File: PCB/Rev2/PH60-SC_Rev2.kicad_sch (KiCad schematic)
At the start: 43 parts, among them J1 USB_C_Receptacle_USB2.0_14P, J2 Conn_01x02_Pin, J3 Conn_01x02_Pin, U1 nRF52840, X1 32.768kHz, X2 Crystal_Generic

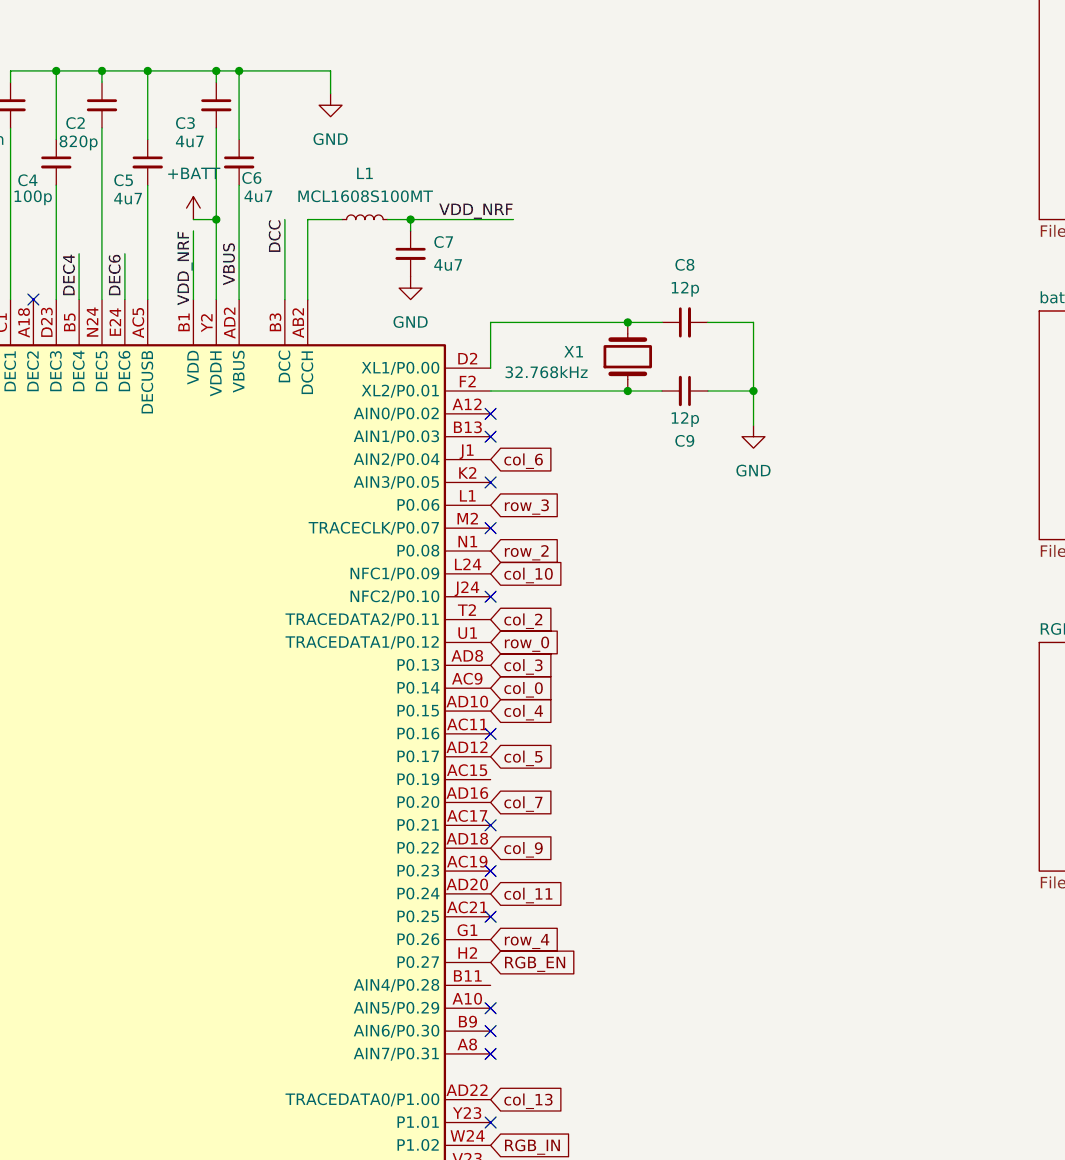
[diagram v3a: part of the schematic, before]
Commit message: 电源模块布局及drc
修改52840的vddh，将batt修改为vdd，TPS2116DRL布局与简单drc，rgb_vdd布局仍需修改
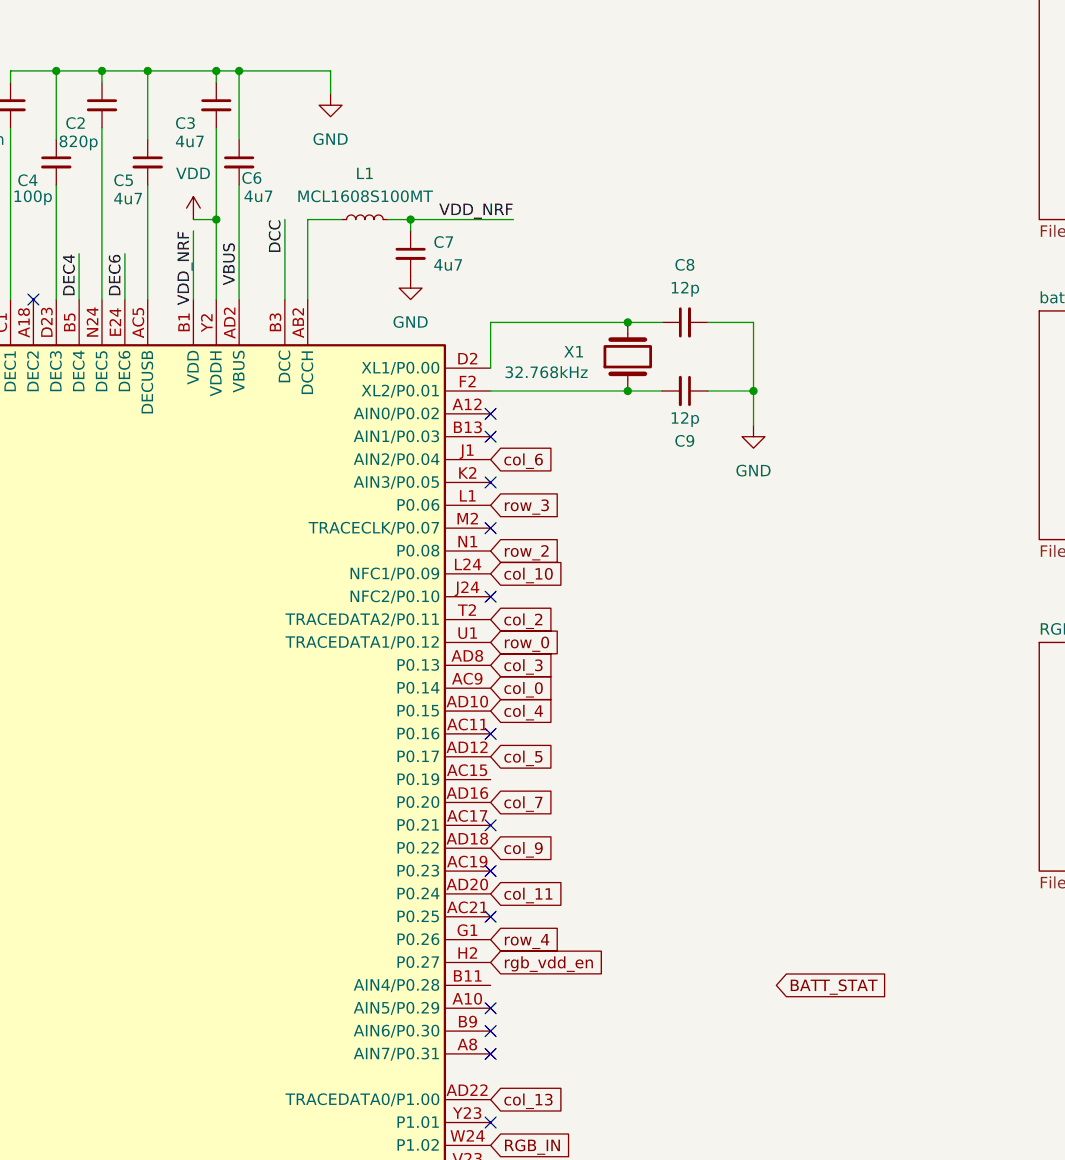
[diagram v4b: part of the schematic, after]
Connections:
- net +BATT renamed VDD
- net RGB_EN renamed rgb_vdd_en
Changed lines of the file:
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@@
 		)
 	)
-	(global_label "RGB_EN"
-		(shape input)
-		(at 256.54 152.4 0)
-		(fields_autoplaced yes)
-		(effects
-			(font
-				(size 1.27 1.27)
-			)
-			(justify left)
-		)
-		(property "Intersheetrefs" "${INTERSHEET_REFS}"
-			(at 266.7823 152.4 0)
-			(effects
-				(font
-					(size 1.27 1.27)
-				)
-				(justify left)
-				(hide yes)
-			)
-		)
-	)
 	(global_label "col_12"
 		(shape input)
@@
 		)
 	)
+	(global_label "BATT_STAT"
+		(shape input)
+		(at 288.29 154.94 0)
+		(fields_autoplaced yes)
+		(effects
+			(font
+				(size 1.27 1.27)
+			)
+			(justify left)
+		)
+		(property "Intersheetrefs" "${INTERSHEET_REFS}"
+			(at 300.7699 154.94 0)
+			(effects
+				(font
+					(size 1.27 1.27)
+				)
+				(justify left)
+				(hide yes)
+			)
+		)
+	)
+	(global_label "rgb_vdd_en"
+		(shape input)
+		(at 256.54 152.4 0)
+		(fields_autoplaced yes)
+		(effects
+			(font
+				(size 1.27 1.27)
+			)
+			(justify left)
+		)
+		(property "Intersheetrefs" "${INTERSHEET_REFS}"
+			(at 270.0478 152.4 0)
+			(effects
+				(font
+					(size 1.27 1.27)
+				)
+				(justify left)
+				(hide yes)
+			)
+		)
+	)
 	(symbol
 		(lib_id "Device:C_Small")
@@
 		(dnp no)
 		(fields_autoplaced yes)
-		(property "Reference" "#PWR015"
+		(property "Reference" "#PWR016"
 			(at 154.94 262.89 0)
 			(effects
@@
 			(project "PH64lite"
 				(path "/dca0f898-8fdb-4522-a51d-f4f4238906e7"
-					(reference "#PWR015")
+					(reference "#PWR016")
 					(unit 1)
 				)
@@
 		(dnp no)
 		(fields_autoplaced yes)
-		(property "Reference" "#PWR016"
+		(property "Reference" "#PWR017"
 			(at 224.79 266.7 0)
 			(effects
@@
 			(project "PH64lite"
 				(path "/dca0f898-8fdb-4522-a51d-f4f4238906e7"
-					(reference "#PWR016")
+					(reference "#PWR017")
 					(unit 1)
 				)
@@
 		(dnp no)
 		(fields_autoplaced yes)
-		(property "Reference" "#PWR013"
+		(property "Reference" "#PWR014"
 			(at 85.09 218.44 0)
 			(effects
@@
 			(project "PH60S lite"
 				(path "/dca0f898-8fdb-4522-a51d-f4f4238906e7"
-					(reference "#PWR013")
+					(reference "#PWR014")
 					(unit 1)
 				)
@@
 		(dnp no)
 		(fields_autoplaced yes)
-		(property "Reference" "#PWR06"
+		(property "Reference" "#PWR07"
 			(at 35.56 105.41 0)
 			(effects
@@
 			(project "PH64lite"
 				(path "/dca0f898-8fdb-4522-a51d-f4f4238906e7"
-					(reference "#PWR06")
-					(unit 1)
-				)
-			)
-		)
-	)
-	(symbol
-		(lib_id "power:+BATT")
-		(at 223.52 69.85 0)
-		(unit 1)
-		(exclude_from_sim no)
-		(in_bom yes)
-		(on_board yes)
-		(dnp no)
-		(fields_autoplaced yes)
-		(property "Reference" "#PWR022"
-			(at 223.52 73.66 0)
-			(effects
-				(font
-					(size 1.27 1.27)
-				)
-				(hide yes)
-			)
-		)
-		(property "Value" "+BATT"
-			(at 223.52 64.77 0)
-			(effects
-				(font
-					(size 1.27 1.27)
-				)
-			)
-		)
-		(property "Footprint" ""
-			(at 223.52 69.85 0)
-			(effects
-				(font
-					(size 1.27 1.27)
-				)
-				(hide yes)
-			)
-		)
-		(property "Datasheet" ""
-			(at 223.52 69.85 0)
-			(effects
-				(font
-					(size 1.27 1.27)
-				)
-				(hide yes)
-			)
-		)
-		(property "Description" "Power symbol creates a global label with name \"+BATT\""
-			(at 223.52 69.85 0)
-			(effects
-				(font
-					(size 1.27 1.27)
-				)
-				(hide yes)
-			)
-		)
-		(pin "1"
-		)
-		(instances
-			(project "PH60-SC_Rev2"
-				(path "/dca0f898-8fdb-4522-a51d-f4f4238906e7"
-					(reference "#PWR022")
+					(reference "#PWR07")
 					(unit 1)
 				)
@@
 		(dnp no)
 		(fields_autoplaced yes)
-		(property "Reference" "#PWR014"
+		(property "Reference" "#PWR015"
 			(at 220.98 232.41 0)
 			(effects
@@
 			(project ""
 				(path "/dca0f898-8fdb-4522-a51d-f4f4238906e7"
-					(reference "#PWR014")
+					(reference "#PWR015")
 					(unit 1)
 				)
@@
 		(dnp no)
 		(fields_autoplaced yes)
-		(property "Reference" "#PWR012"
+		(property "Reference" "#PWR013"
 			(at 175.26 210.82 0)
 			(effects
@@
 			(project "PH64lite"
 				(path "/dca0f898-8fdb-4522-a51d-f4f4238906e7"
-					(reference "#PWR012")
+					(reference "#PWR013")
 					(unit 1)
 				)
@@
 		(dnp no)
 		(fields_autoplaced yes)
-		(property "Reference" "#PWR08"
+		(property "Reference" "#PWR09"
 			(at 158.75 163.83 0)
 			(effects
@@
 			(project "PH64lite"
 				(path "/dca0f898-8fdb-4522-a51d-f4f4238906e7"
-					(reference "#PWR08")
+					(reference "#PWR09")
 					(unit 1)
 				)
@@
 		(dnp no)
 		(fields_autoplaced yes)
-		(property "Reference" "#PWR019"
+		(property "Reference" "#PWR011"
 			(at 350.52 184.15 0)
 			(effects
@@
 			(project "PH60-SC_Rev2"
 				(path "/dca0f898-8fdb-4522-a51d-f4f4238906e7"
-					(reference "#PWR019")
+					(reference "#PWR011")
 					(unit 1)
 				)
@@
 		(dnp no)
 		(fields_autoplaced yes)
-		(property "Reference" "#PWR011"
+		(property "Reference" "#PWR012"
 			(at 363.22 191.77 0)
 			(effects
@@
 			(project ""
 				(path "/dca0f898-8fdb-4522-a51d-f4f4238906e7"
-					(reference "#PWR011")
+					(reference "#PWR012")
 					(unit 1)
 				)
@@
 		(dnp no)
 		(fields_autoplaced yes)
-		(property "Reference" "#PWR04"
+		(property "Reference" "#PWR05"
 			(at 247.65 82.55 0)
 			(effects
@@
 			(project "PH64lite"
 				(path "/dca0f898-8fdb-4522-a51d-f4f4238906e7"
-					(reference "#PWR04")
+					(reference "#PWR05")
 					(unit 1)
 				)
@@
 		(dnp no)
 		(fields_autoplaced yes)
-		(property "Reference" "#PWR05"
+		(property "Reference" "#PWR06"
 			(at 285.75 99.06 0)
 			(effects
@@
 			(project "PH64lite"
 				(path "/dca0f898-8fdb-4522-a51d-f4f4238906e7"
-					(reference "#PWR05")
+					(reference "#PWR06")
 					(unit 1)
 				)
@@
 		(dnp no)
 		(fields_autoplaced yes)
-		(property "Reference" "#PWR09"
+		(property "Reference" "#PWR010"
 			(at 85.09 185.42 0)
 			(effects
@@
 			(project "PH60-SC_Rev2"
 				(path "/dca0f898-8fdb-4522-a51d-f4f4238906e7"
-					(reference "#PWR09")
+					(reference "#PWR010")
 					(unit 1)
 				)
@@
 		(dnp no)
 		(fields_autoplaced yes)
-		(property "Reference" "#FLG05"
+		(property "Reference" "#FLG01"
 			(at 346.71 186.055 0)
 			(effects
@@
 			(project "PH60-SC_Rev2"
 				(path "/dca0f898-8fdb-4522-a51d-f4f4238906e7"
-					(reference "#FLG05")
+					(reference "#FLG01")
 					(unit 1)
 				)
@@
 	)
 	(symbol
+		(lib_id "power:VDD")
+		(at 223.52 69.85 0)
+		(unit 1)
+		(exclude_from_sim no)
+		(in_bom yes)
+		(on_board yes)
+		(dnp no)
+		(fields_autoplaced yes)
+		(property "Reference" "#PWR04"
+			(at 223.52 73.66 0)
+			(effects
+				(font
+					(size 1.27 1.27)
+				)
+				(hide yes)
+			)
+		)
+		(property "Value" "VDD"
+			(at 223.52 64.77 0)
+			(effects
+				(font
+					(size 1.27 1.27)
+				)
+			)
+		)
+		(property "Footprint" ""
+			(at 223.52 69.85 0)
+			(effects
+				(font
+					(size 1.27 1.27)
+				)
+				(hide yes)
+			)
+		)
+		(property "Datasheet" ""
+			(at 223.52 69.85 0)
+			(effects
+				(font
+					(size 1.27 1.27)
+				)
+				(hide yes)
+			)
+		)
+		(property "Description" "Power symbol creates a global label with name \"VDD\""
+			(at 223.52 69.85 0)
+			(effects
+				(font
+					(size 1.27 1.27)
+				)
+				(hide yes)
+			)
+		)
+		(pin "1"
+		)
+		(instances
+			(project "PH60-SC_Rev2"
+				(path "/dca0f898-8fdb-4522-a51d-f4f4238906e7"
+					(reference "#PWR04")
+					(unit 1)
+				)
+			)
+		)
+	)
+	(symbol
 		(lib_id "power:GND")
 		(at 156.21 114.3 0)
@@
 		(dnp no)
 		(fields_autoplaced yes)
-		(property "Reference" "#PWR07"
+		(property "Reference" "#PWR08"
 			(at 156.21 120.65 0)
 			(effects
@@
 			(project "PH64lite"
 				(path "/dca0f898-8fdb-4522-a51d-f4f4238906e7"
-					(reference "#PWR07")
+					(reference "#PWR08")
 					(unit 1)
 				)

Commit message: sc2最终审核（nayat）
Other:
- note added: "ESD"
- note added: "USB"
- moved on the sheet: C14, C15, C16, C17, C18, C19, C20, D1, J1, J2, J3, L3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

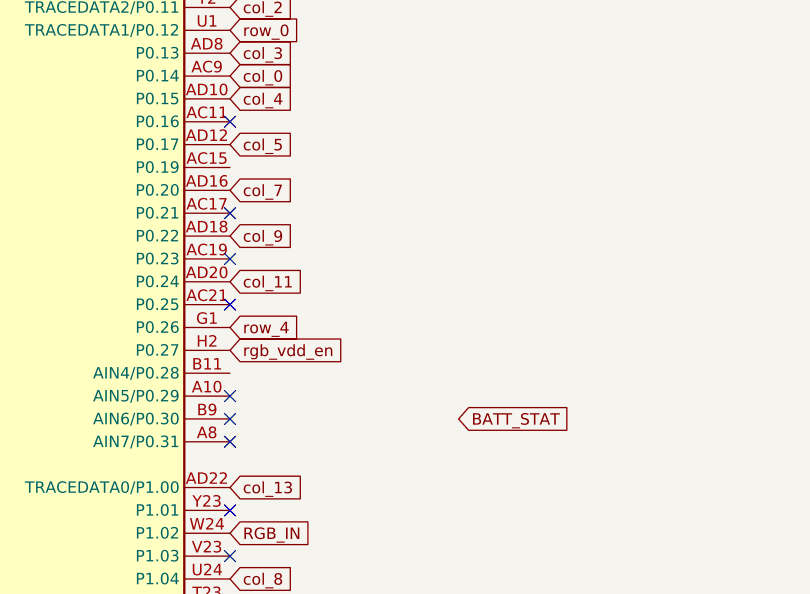
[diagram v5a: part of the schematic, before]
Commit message: Fix RGB_VDD
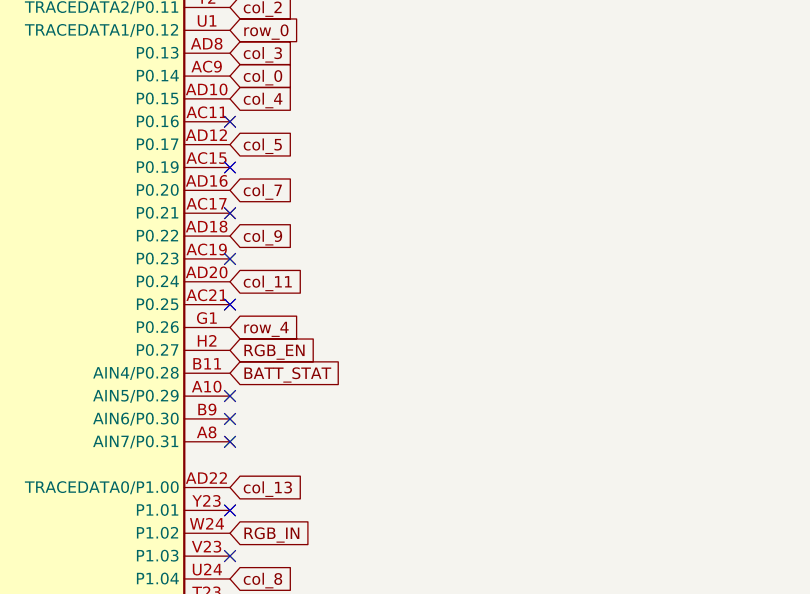
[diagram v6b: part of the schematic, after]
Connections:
- net BATT_STAT: now also U1.B11 (AIN4/P0.28)
- net rgb_vdd_en renamed RGB_EN
- no-connect marks 23 -> 24
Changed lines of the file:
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@@
+	)
+	(no_connect
+		(at 256.54 132.08)
 	)
 	(no_connect
@@
 	(global_label "BATT_STAT"
 		(shape input)
-		(at 281.94 160.02 0)
-		(fields_autoplaced yes)
-		(effects
-			(font
-				(size 1.27 1.27)
-			)
-			(justify left)
-		)
-		(property "Intersheetrefs" "${INTERSHEET_REFS}"
-			(at 294.4199 160.02 0)
+		(at 256.54 154.94 0)
+		(fields_autoplaced yes)
+		(effects
+			(font
+				(size 1.27 1.27)
+			)
+			(justify left)
+		)
+		(property "Intersheetrefs" "${INTERSHEET_REFS}"
+			(at 269.0199 154.94 0)
 			(effects
 				(font
@@
 		)
 	)
-	(global_label "rgb_vdd_en"
+	(global_label "RGB_EN"
 		(shape input)
 		(at 256.54 152.4 0)
@@
 		)
 		(property "Intersheetrefs" "${INTERSHEET_REFS}"
-			(at 270.0478 152.4 0)
-			(effects
-				(font
+			(at 266.7823 152.4 0)
+			(effects
+				(font

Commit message: layout and drc
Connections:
- net BATT_STAT: now also U1.Y23 (P1.01); no longer U1.B11 (AIN4/P0.28)
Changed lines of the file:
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@@
+	)
+	(no_connect
+		(at 256.54 205.74)
+	)
+	(no_connect
+		(at 256.54 193.04)
+	)
+	(no_connect
+		(at 256.54 198.12)
+	)
+	(no_connect
+		(at 205.74 78.74)
+	)
+	(no_connect
+		(at 256.54 154.94)
+	)
+	(no_connect
+		(at 256.54 203.2)
+	)
+	(no_connect
+		(at 256.54 175.26)
+	)
+	(no_connect
+		(at 256.54 180.34)
+	)
+	(no_connect
+		(at 256.54 137.16)
+	)
+	(no_connect
+		(at 256.54 93.98)
 	)
 	(no_connect
@@
 	)
 	(no_connect
-		(at 256.54 205.74)
-	)
-	(no_connect
-		(at 256.54 193.04)
-	)
-	(no_connect
-		(at 256.54 198.12)
-	)
-	(no_connect
-		(at 205.74 78.74)
-	)
-	(no_connect
-		(at 256.54 203.2)
-	)
-	(no_connect
-		(at 256.54 175.26)
-	)
-	(no_connect
-		(at 256.54 180.34)
-	)
-	(no_connect
-		(at 256.54 137.16)
-	)
-	(no_connect
-		(at 256.54 93.98)
-	)
-	(no_connect
 		(at 256.54 104.14)
 	)
 	(no_connect
 		(at 256.54 99.06)
-	)
-	(no_connect
-		(at 256.54 170.18)
 	)
 	(no_connect
@@
 		)
 	)
-	(global_label "BATT_STAT"
-		(shape input)
-		(at 256.54 154.94 0)
-		(fields_autoplaced yes)
-		(effects
-			(font
-				(size 1.27 1.27)
-			)
-			(justify left)
-		)
-		(property "Intersheetrefs" "${INTERSHEET_REFS}"
-			(at 269.0199 154.94 0)
+	(global_label "RGB_EN"
+		(shape input)
+		(at 256.54 152.4 0)
+		(fields_autoplaced yes)
+		(effects
+			(font
+				(size 1.27 1.27)
+			)
+			(justify left)
+		)
+		(property "Intersheetrefs" "${INTERSHEET_REFS}"
+			(at 266.7823 152.4 0)
 			(effects
 				(font
@@
 		)
 	)
-	(global_label "RGB_EN"
-		(shape input)
-		(at 256.54 152.4 0)
-		(fields_autoplaced yes)
-		(effects
-			(font
-				(size 1.27 1.27)
-			)
-			(justify left)
-		)
-		(property "Intersheetrefs" "${INTERSHEET_REFS}"
-			(at 266.7823 152.4 0)
-			(effects
-				(font
+	(global_label "BATT_STAT"
+		(shape input)
+		(at 256.54 170.18 0)
+		(fields_autoplaced yes)
+		(effects
+			(font
+				(size 1.27 1.27)
+			)
+			(justify left)
+		)
+		(property "Intersheetrefs" "${INTERSHEET_REFS}"
+			(at 269.0199 170.18 0)
+			(effects
+				(font
